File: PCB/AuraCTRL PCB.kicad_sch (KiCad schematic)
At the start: 1 part, among them U1 ESP32-C3-DevKitM-1

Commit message: Pcb, schematic, and journal of june 13
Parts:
- removed U1: ESP32-C3-DevKitM-1, RF_Module:ESP32-C3-DevKitM-1, symbol RF_Module:ESP32-C3-DevKitM-1
- added Back1, Confirm1, D-Pad_Right1, D-Pad_Up1, Enter1, SW5, SW6, SW7, SW8: SW_Push, Button_Switch_THT:SW_PUSH_6mm, symbol Switch:SW_Push
- added D1, D2, D3, D4, D5, D6, D7: SK6812MINI, libs:SK6812-MINI-E, symbol LED:SK6812MINI
- added SW1: RotaryEncoder_Switch, Rotary_Encoder:RotaryEncoder_Alps_EC11E-Switch_Vertical_H20mm, symbol Device:RotaryEncoder_Switch
- added U1: XIAO-ESP32-C3-DIP, Seeed Studio XIAO Series Library:XIAO-ESP32C3-DIP, symbol Seeed_Studio_XIAO_Series:XIAO-ESP32-C3-DIP
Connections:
- new net: D4.1 (DOUT), D5.3 (DIN)
- new net: D1.2 (VSS), D2.2 (VSS), D3.2 (VSS), D4.2 (VSS), D5.2 (VSS), D6.2 (VSS), D7.2 (VSS)
- new net: D3.1 (DOUT), D4.3 (DIN)
- new net: D1.4 (VDD), D2.4 (VDD), D3.4 (VDD), D4.4 (VDD), D5.4 (VDD), D6.4 (VDD), D7.4 (VDD)
- new net: D6.1 (DOUT), D7.1 (DOUT)
- new net: D2.1 (DOUT), D3.3 (DIN)
- new net: D5.1 (DOUT), D6.3 (DIN)
- new net: D1.1 (DOUT), D2.3 (DIN)
- new net: D1.3 (DIN), U1.1 (GPIO2/A0/D0)
- new net 5V+: U1.14 (VBUS)
- new net Colum1: Confirm1.1, D-Pad_Right1.1, SW5.1, U1.2 (GPIO3/A1/D1)
- new net Colum2: D-Pad_Up1.1, Enter1.1, SW6.1, U1.3 (GPIO4/A2/D2)
- new net Colum3: Back1.1, SW1.S1, SW7.1, SW8.1, U1.4 (GPIO5/A3/D3)
- new net EC-A: SW1.A, U1.7 (GPIO21/D6/TX)
- new net EC-B: SW1.B, U1.8 (GPIO20/D7/RX)
- new net GND: SW1.C, U1.13 (GND)
- new net Row1: Back1.2, Confirm1.2, D-Pad_Up1.2, SW1.S2, U1.11 (GPIO10/D10/MOSI)
- new net Row2: D-Pad_Right1.2, Enter1.2, SW7.2, U1.10 (GPIO9/D9/MISO)
- new net Row3: SW5.2, SW6.2, SW8.2, U1.9 (GPIO8/D8/SCK)

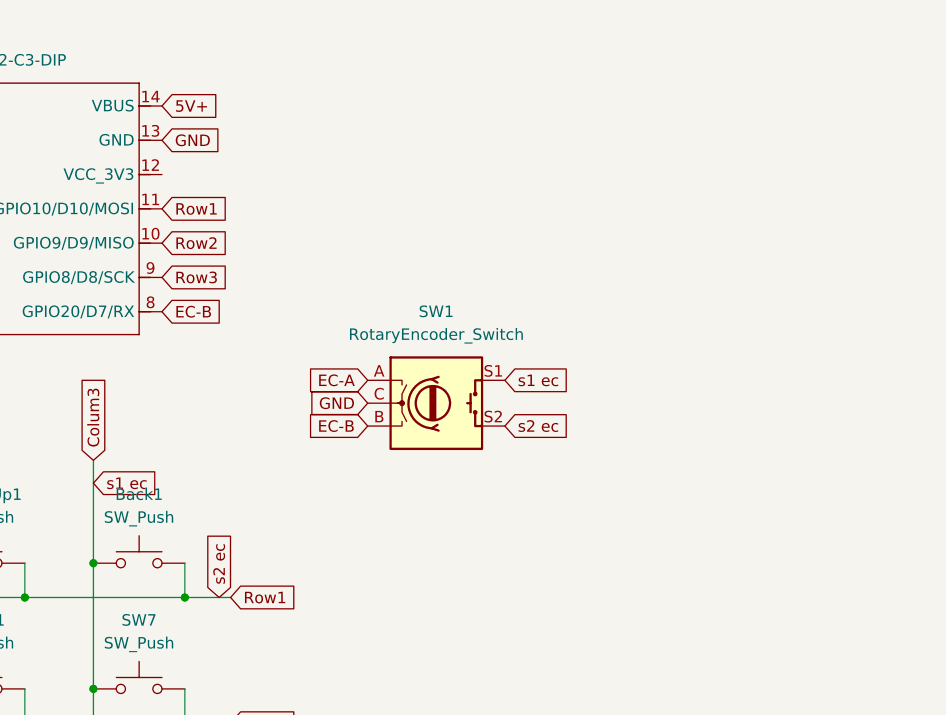
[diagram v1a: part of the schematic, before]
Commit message: added the display, rewired neopixels, pcb outline
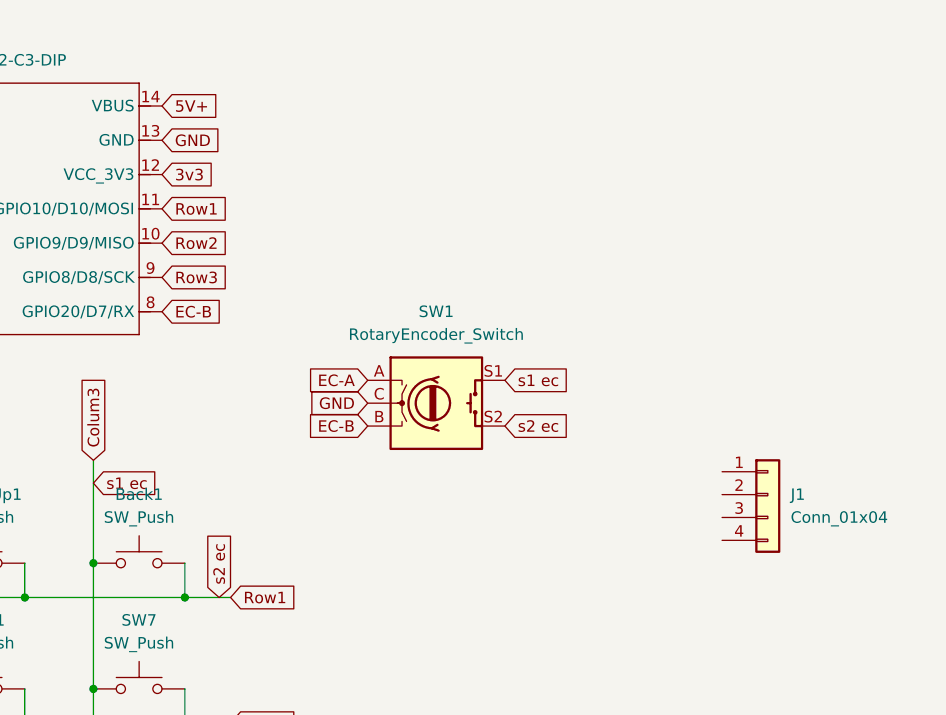
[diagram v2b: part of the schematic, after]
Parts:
- added J1: Conn_01x04, libs:128x64OLED, symbol Connector_Generic:Conn_01x04
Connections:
- net 3v3: now reaches U1.12 (VCC_3V3)
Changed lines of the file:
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@@
+		)
+	)
+	(global_label "3v3"
+		(shape input)
+		(at 160.02 72.39 0)
+		(fields_autoplaced yes)
+		(effects
+			(font
+				(size 1.27 1.27)
+			)
+			(justify left)
+		)
+		(property "Intersheetrefs" "${INTERSHEET_REFS}"
+			(at 166.3918 72.39 0)
+			(effects
+				(font
+					(size 1.27 1.27)
+				)
+				(justify left)
+				(hide yes)
+			)
 		)
 	)
@@
 					(unit 1)
 				)
+			)
+		)
+	)
+	(symbol
+		(lib_id "Connector_Generic:Conn_01x04")
+		(at 227.33 107.95 0)
+		(unit 1)
+		(exclude_from_sim no)
+		(in_bom yes)
+		(on_board yes)
+		(dnp no)
+		(fields_autoplaced yes)
+		(property "Reference" "J1"
+			(at 229.87 107.9499 0)
+			(effects
+				(font
+					(size 1.27 1.27)
+				)
+				(justify left)
+			)
+		)
+		(property "Value" "Conn_01x04"
+			(at 229.87 110.4899 0)
+			(effects
+				(font
+					(size 1.27 1.27)
+				)
+				(justify left)
+			)
+		)
+		(property "Footprint" "libs:128x64OLED"
+			(at 227.33 107.95 0)
+			(effects
+				(font
+					(size 1.27 1.27)
+				)
+				(hide yes)
+			)
+		)
+		(property "Datasheet" "~"
+			(at 227.33 107.95 0)
+			(effects
+				(font
+					(size 1.27 1.27)
+				)
+				(hide yes)
+			)
+		)
+		(property "Description" "Generic connector, single row, 01x04, script generated (kicad-library-utils/schlib/autogen/connector/)"
+			(at 227.33 107.95 0)
+			(effects
+				(font
+					(size 1.27 1.27)
+				)
+				(hide yes)
+			)
+		)
+		(pin "1"
+		)
+		(pin "3"
+		)
+		(pin "4"
+		)
+		(pin "2"
+		)
+		(instances
+			(project ""
+				(path "/e1040f08-0fe8-443b-853b-78c16d89340a"
+					(reference "J1")
+					(unit 1)
+				)
